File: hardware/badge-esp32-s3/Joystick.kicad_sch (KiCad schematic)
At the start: 1 part

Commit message: Annotate schematic
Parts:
- renumbered S2 to S1
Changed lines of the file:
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@@
 		(dnp no)
 		(fields_autoplaced yes)
-		(property "Reference" "#PWR037"
+		(property "Reference" "#PWR057"
 			(at 147.32 95.25 0)
 			(effects
@@
 			(project ""
 				(path "/e2af9a6c-dbe9-4de2-9ba6-ea213a7300ec/9feb22ac-0492-47b5-89fe-3e77a54de168/0e604a77-d00c-4663-aa0e-d86b906e110e"
-					(reference "#PWR037")
+					(reference "#PWR057")
 					(unit 1)
 				)
@@
 		(dnp no)
 		(fields_autoplaced yes)
-		(property "Reference" "S2"
+		(property "Reference" "S1"
 			(at 128.27 85.09 0)
 			(effects
@@
 			(project ""
 				(path "/e2af9a6c-dbe9-4de2-9ba6-ea213a7300ec/9feb22ac-0492-47b5-89fe-3e77a54de168/0e604a77-d00c-4663-aa0e-d86b906e110e"
-					(reference "S2")
+					(reference "S1")
 					(unit 2)
 				)
@@
 		(dnp no)
 		(fields_autoplaced yes)
-		(property "Reference" "S2"
+		(property "Reference" "S1"
 			(at 101.6 85.09 0)
 			(effects
@@
 			(project ""
 				(path "/e2af9a6c-dbe9-4de2-9ba6-ea213a7300ec/9feb22ac-0492-47b5-89fe-3e77a54de168/0e604a77-d00c-4663-aa0e-d86b906e110e"
-					(reference "S2")
+					(reference "S1")
 					(unit 1)
 				)

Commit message: Update Joystick.kicad_sch
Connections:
- net 3.3vin: now also S1.X-, S1.Y-; no longer S1.X-, S1.Y-
- net GND: now also S1.X+, S1.Y+; no longer S1.X+, S1.Y+
- removed net Xout(analoge): S1.X
- removed net Yout(analoge: S1.Y
- new net Xout(analog): S1.Y
- new net Yout(analog): S1.X

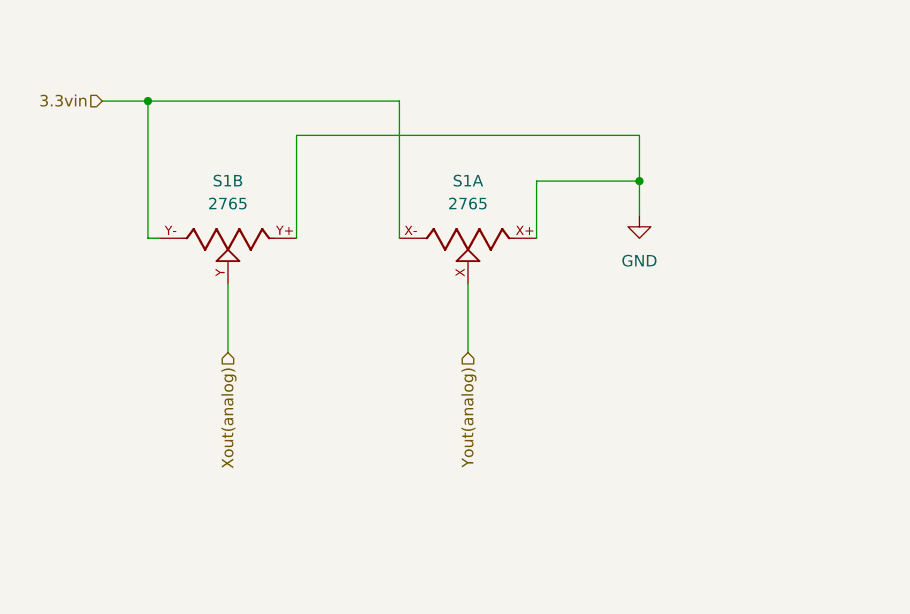
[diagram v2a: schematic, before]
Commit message: changed joystick and fixed minibadge in the schematic
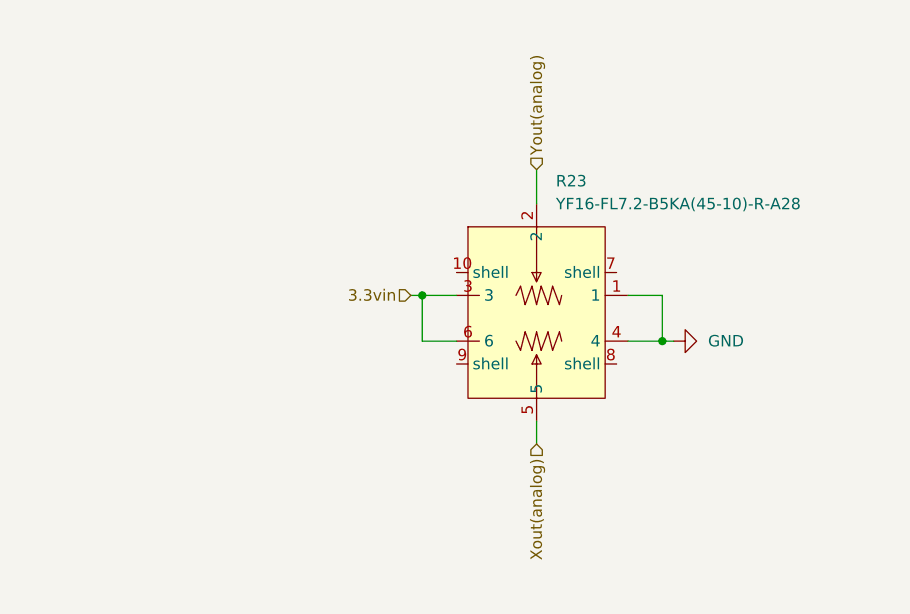
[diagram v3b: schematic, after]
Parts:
- removed S1: 2765, AdafruitJoystick:SW_2765, symbol AdafruitJoystick:2765
- added R23: YF16-FL7.2-B5KA(45-10)-R-A28, lcsc-lib:JOYTICK-TH_YF16-DFL7.2-B5KO-45-10-B5KO-55--RG-A22, symbol lcsc-lib:YF16-FL7.2-B5KA(45-10)-R-A28
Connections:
- net 3.3vin: now also R23.3, R23.6
- net GND: now also R23.1, R23.4
- net Xout(analog): now also R23.5
- net Yout(analog): now also R23.2

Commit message: added sdio
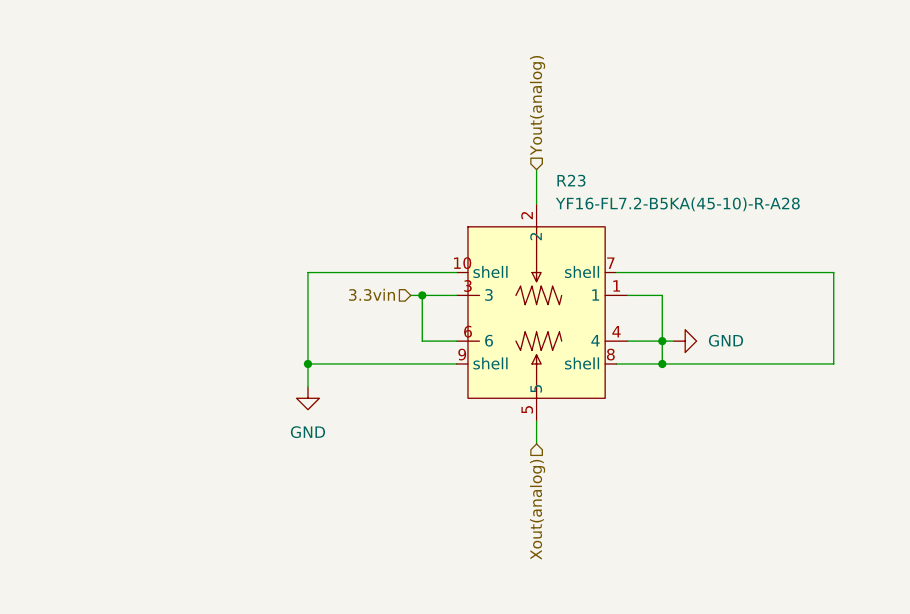
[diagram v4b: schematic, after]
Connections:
- net GND: now also R23.10 (shell), R23.7 (shell), R23.8 (shell), R23.9 (shell)
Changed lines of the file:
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@@
 	(paper "A4")
 	(junction
+		(at 110.49 105.41)
+		(diameter 0)
+		(color 0 0 0 0)
+	)
+	(junction
 		(at 123.19 97.79)
 		(diameter 0)
@@
 		(color 0 0 0 0)
 	)
+	(junction
+		(at 149.86 105.41)
+		(diameter 0)
+		(color 0 0 0 0)
+	)
+	(wire
+		(pts
+			(xy 110.49 105.41) (xy 127 105.41)
+		)
+		(stroke
+			(width 0)
+			(type default)
+		)
+	)
 	(wire
 		(pts
@@
 	(wire
 		(pts
+			(xy 144.78 95.25) (xy 168.91 95.25)
+		)
+		(stroke
+			(width 0)
+			(type default)
+		)
+	)
+	(wire
+		(pts
 			(xy 123.19 97.79) (xy 123.19 102.87)
 		)
@@
 	(wire
 		(pts
+			(xy 149.86 105.41) (xy 168.91 105.41)
+		)
+		(stroke
+			(width 0)
+			(type default)
+		)
+	)
+	(wire
+		(pts
+			(xy 149.86 102.87) (xy 149.86 105.41)
+		)
+		(stroke
+			(width 0)
+			(type default)
+		)
+	)
+	(wire
+		(pts
 			(xy 149.86 102.87) (xy 151.13 102.87)
 		)
@@
 	(wire
 		(pts
+			(xy 144.78 105.41) (xy 149.86 105.41)
+		)
+		(stroke
+			(width 0)
+			(type default)
+		)
+	)
+	(wire
+		(pts
 			(xy 135.89 111.76) (xy 135.89 114.3)
+		)
+		(stroke
+			(width 0)
+			(type default)
+		)
+	)
+	(wire
+		(pts
+			(xy 127 95.25) (xy 110.49 95.25)
+		)
+		(stroke
+			(width 0)
+			(type default)
+		)
+	)
+	(wire
+		(pts
+			(xy 168.91 95.25) (xy 168.91 105.41)
+		)
+		(stroke
+			(width 0)
+			(type default)
+		)
+	)
+	(wire
+		(pts
+			(xy 110.49 95.25) (xy 110.49 105.41)
+		)
+		(stroke
+			(width 0)
+			(type default)
+		)
+	)
+	(wire
+		(pts
+			(xy 110.49 105.41) (xy 110.49 107.95)
 		)
 		(stroke
@@
 		)
 	)
+	(symbol
+		(lib_id "power:GND")
+		(at 110.49 107.95 0)
+		(unit 1)
+		(exclude_from_sim no)
+		(in_bom yes)
+		(on_board yes)
+		(dnp no)
+		(fields_autoplaced yes)
+		(property "Reference" "#PWR042"
+			(at 110.49 114.3 0)
+			(effects
+				(font
+					(size 1.27 1.27)
+				)
+				(hide yes)
+			)
+		)
+		(property "Value" "GND"
+			(at 110.49 113.03 0)
+			(effects
+				(font
+					(size 1.27 1.27)
+				)
+			)
+		)
+		(property "Footprint" ""
+			(at 110.49 107.95 0)
+			(effects
+				(font
+					(size 1.27 1.27)
+				)
+				(hide yes)
+			)
+		)
+		(property "Datasheet" ""
+			(at 110.49 107.95 0)
+			(effects
+				(font
+					(size 1.27 1.27)
+				)
+				(hide yes)
+			)
+		)
+		(property "Description" "Power symbol creates a global label with name \"GND\" , ground"
+			(at 110.49 107.95 0)
+			(effects
+				(font
+					(size 1.27 1.27)
+				)
+				(hide yes)
+			)
+		)
+		(pin "1"
+		)
+		(instances
+			(project ""
+				(path "/e2af9a6c-dbe9-4de2-9ba6-ea213a7300ec/9feb22ac-0492-47b5-89fe-3e77a54de168/0e604a77-d00c-4663-aa0e-d86b906e110e"
+					(reference "#PWR042")
+					(unit 1)
+				)
+			)
+		)
+	)

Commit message: almost finished
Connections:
- net 3.3vin: now also R23.4; no longer R23.6
- net GND: now also R23.6; no longer R23.4
- net Xout(analog): now also R23.2; no longer R23.5
- net Yout(analog): now also R23.5; no longer R23.2
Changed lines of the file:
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@@
 	)
 	(junction
-		(at 123.19 97.79)
+		(at 148.59 95.25)
 		(diameter 0)
 		(color 0 0 0 0)
 	)
 	(junction
-		(at 149.86 102.87)
+		(at 124.46 105.41)
 		(diameter 0)
 		(color 0 0 0 0)
 	)
 	(junction
-		(at 149.86 105.41)
+		(at 168.91 105.41)
 		(diameter 0)
 		(color 0 0 0 0)
@@
 	(wire
 		(pts
-			(xy 110.49 105.41) (xy 127 105.41)
-		)
-		(stroke
-			(width 0)
-			(type default)
-		)
-	)
-	(wire
-		(pts
-			(xy 149.86 97.79) (xy 149.86 102.87)
-		)
-		(stroke
-			(width 0)
-			(type default)
-		)
-	)
-	(wire
-		(pts
-			(xy 127 97.79) (xy 123.19 97.79)
+			(xy 121.92 97.79) (xy 127 97.79)
 		)
 		(stroke
@@
 	(wire
 		(pts
-			(xy 144.78 95.25) (xy 168.91 95.25)
-		)
-		(stroke
-			(width 0)
-			(type default)
-		)
-	)
-	(wire
-		(pts
-			(xy 123.19 97.79) (xy 123.19 102.87)
-		)
-		(stroke
-			(width 0)
-			(type default)
-		)
-	)
-	(wire
-		(pts
-			(xy 121.92 97.79) (xy 123.19 97.79)
-		)
-		(stroke
-			(width 0)
-			(type default)
-		)
-	)
-	(wire
-		(pts
-			(xy 146.05 102.87) (xy 149.86 102.87)
-		)
-		(stroke
-			(width 0)
-			(type default)
-		)
-	)
-	(wire
-		(pts
-			(xy 149.86 105.41) (xy 168.91 105.41)
-		)
-		(stroke
-			(width 0)
-			(type default)
-		)
-	)
-	(wire
-		(pts
-			(xy 149.86 102.87) (xy 149.86 105.41)
-		)
-		(stroke
-			(width 0)
-			(type default)
-		)
-	)
-	(wire
-		(pts
-			(xy 149.86 102.87) (xy 151.13 102.87)
-		)
-		(stroke
-			(width 0)
-			(type default)
-		)
-	)
-	(wire
-		(pts
-			(xy 144.78 105.41) (xy 149.86 105.41)
+			(xy 144.78 95.25) (xy 148.59 95.25)
+		)
+		(stroke
+			(width 0)
+			(type default)
+		)
+	)
+	(wire
+		(pts
+			(xy 127 102.87) (xy 124.46 102.87)
+		)
+		(stroke
+			(width 0)
+			(type default)
+		)
+	)
+	(wire
+		(pts
+			(xy 124.46 102.87) (xy 124.46 105.41)
+		)
+		(stroke
+			(width 0)
+			(type default)
+		)
+	)
+	(wire
+		(pts
+			(xy 168.91 105.41) (xy 168.91 107.95)
+		)
+		(stroke
+			(width 0)
+			(type default)
+		)
+	)
+	(wire
+		(pts
+			(xy 144.78 105.41) (xy 168.91 105.41)
+		)
+		(stroke
+			(width 0)
+			(type default)
+		)
+	)
+	(wire
+		(pts
+			(xy 146.05 102.87) (xy 151.13 102.87)
 		)
 		(stroke
@@
 	(wire
 		(pts
+			(xy 124.46 105.41) (xy 127 105.41)
+		)
+		(stroke
+			(width 0)
+			(type default)
+		)
+	)
+	(wire
+		(pts
 			(xy 168.91 95.25) (xy 168.91 105.41)
 		)
@@
 	(wire
 		(pts
+			(xy 110.49 105.41) (xy 124.46 105.41)
+		)
+		(stroke
+			(width 0)
+			(type default)
+		)
+	)
+	(wire
+		(pts
 			(xy 110.49 95.25) (xy 110.49 105.41)
 		)
@@
 	(wire
 		(pts
+			(xy 148.59 95.25) (xy 168.91 95.25)
+		)
+		(stroke
+			(width 0)
+			(type default)
+		)
+	)
+	(wire
+		(pts
+			(xy 146.05 97.79) (xy 148.59 97.79)
+		)
+		(stroke
+			(width 0)
+			(type default)
+		)
+	)
+	(wire
+		(pts
 			(xy 110.49 105.41) (xy 110.49 107.95)
 		)
@@
 	(wire
 		(pts
-			(xy 123.19 102.87) (xy 127 102.87)
-		)
-		(stroke
-			(width 0)
-			(type default)
-		)
-	)
-	(wire
-		(pts
-			(xy 146.05 97.79) (xy 149.86 97.79)
+			(xy 148.59 97.79) (xy 148.59 95.25)
 		)
 		(stroke
@@
 	(hierarchical_label "Xout(analog)"
 		(shape input)
+		(at 135.89 83.82 90)
+		(effects
+			(font
+				(size 1.27 1.27)
+			)
+			(justify left)
+		)
+	)
+	(hierarchical_label "3.3vin"
+		(shape input)
+		(at 151.13 102.87 0)
+		(effects
+			(font
+				(size 1.27 1.27)
+			)
+			(justify left)
+		)
+	)
+	(hierarchical_label "Yout(analog)"
+		(shape input)
 		(at 135.89 114.3 270)
 		(effects
@@
 			)
 			(justify right)
-		)
-	)
-	(hierarchical_label "Yout(analog)"
-		(shape input)
-		(at 135.89 83.82 90)
-		(effects
-			(font
-				(size 1.27 1.27)
-			)
-			(justify left)
 		)
 	)
@@
 	(symbol
 		(lib_id "power:GND")
-		(at 151.13 102.87 90)
+		(at 168.91 107.95 0)
 		(unit 1)
 		(exclude_from_sim no)
@@
 		(fields_autoplaced yes)
 		(property "Reference" "#PWR057"
-			(at 157.48 102.87 0)
+			(at 168.91 114.3 0)
 			(effects
 				(font
@@
 		)
 		(property "Value" "GND"
-			(at 154.94 102.8699 90)
-			(effects
-				(font
-					(size 1.27 1.27)
-				)
-				(justify right)
+			(at 168.91 113.03 0)
+			(effects
+				(font
+					(size 1.27 1.27)
+				)
 			)
 		)
 		(property "Footprint" ""
-			(at 151.13 102.87 0)
+			(at 168.91 107.95 0)
 			(effects
 				(font
@@
 		)
 		(property "Datasheet" ""
-			(at 151.13 102.87 0)
+			(at 168.91 107.95 0)
 			(effects
 				(font
@@
 		)
 		(property "Description" "Power symbol creates a global label with name \"GND\" , ground"
-			(at 151.13 102.87 0)
-			(effects
-				(font
+			(at 168.91 107.95 0)
+			(effects
+				(font

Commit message: finished component alignment
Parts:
- R23: FT Position Offset (none) -> 0.1905,0.1905
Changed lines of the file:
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@@
+			)
+		)
+		(property "FT Position Offset" "0.1905,0.1905"
+			(at 135.89 100.33 0)
+			(effects
+				(font
+					(size 1.27 1.27)
+				)
+				(hide yes)
 			)
 		)
